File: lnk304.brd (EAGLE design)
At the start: 46 x 24 mm, 19 parts, among them IC1 TPS774, IC2 MCP1703CB

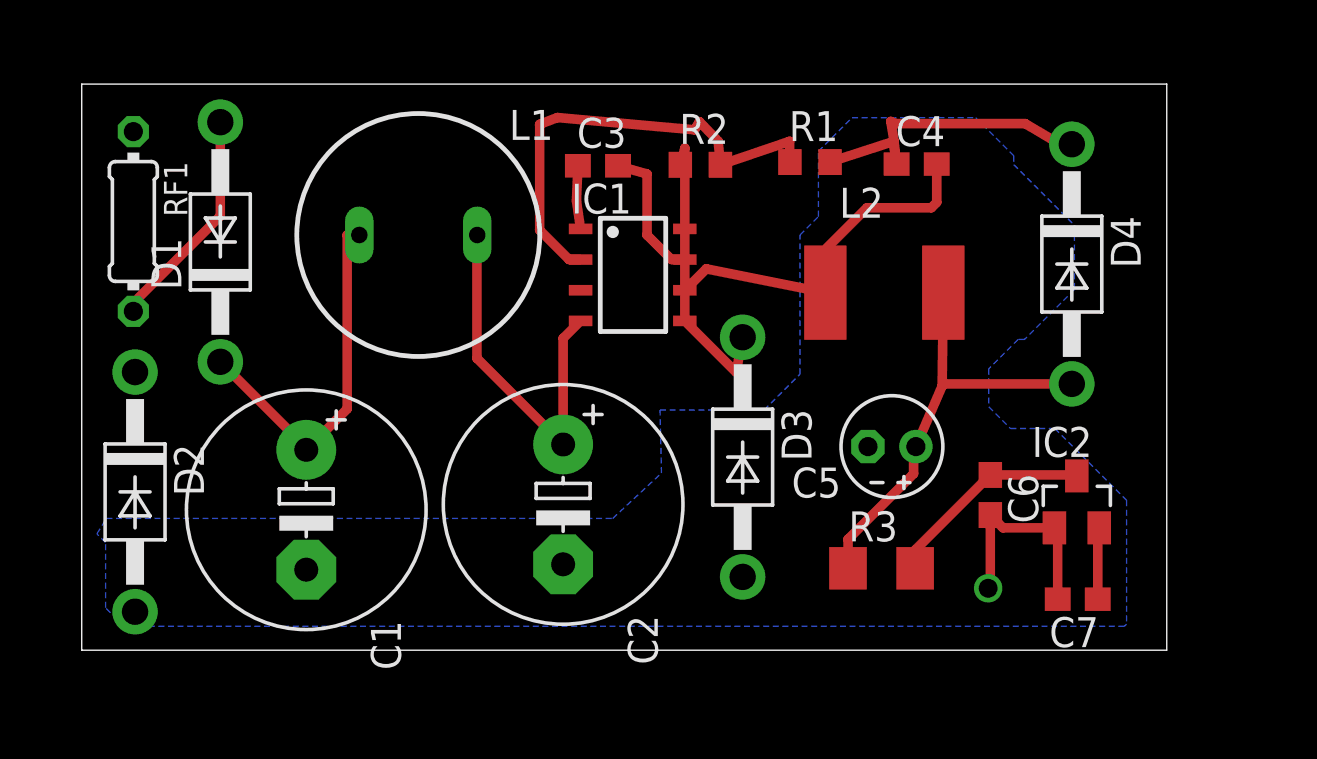
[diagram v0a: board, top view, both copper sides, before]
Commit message: Redesign to add Controller above the converter using pin headers
** 19.Mar.2016 **
Schematic:
- Change RF1 to fuse component
- Added Controller pin headers

PCB Layout:
- Increase board length from 46mm to 49.5mm
- Re orientation of components
RF1, D1, C1, C2, L2 R3 are the main components which were moved for long
distance
- Added Common Plane for Source pin of LNK

-- Missing --
- Need to revise Terminal Block size and overlapping with D2
- The LNK layout used till now is not the correct one.
- May need to increase L2 pad distance a bit
- May need to decrease the board height by 2mm

NOTE: Till now the design is just a fast draft. You can see that some
traces are not drawn in a clean way.
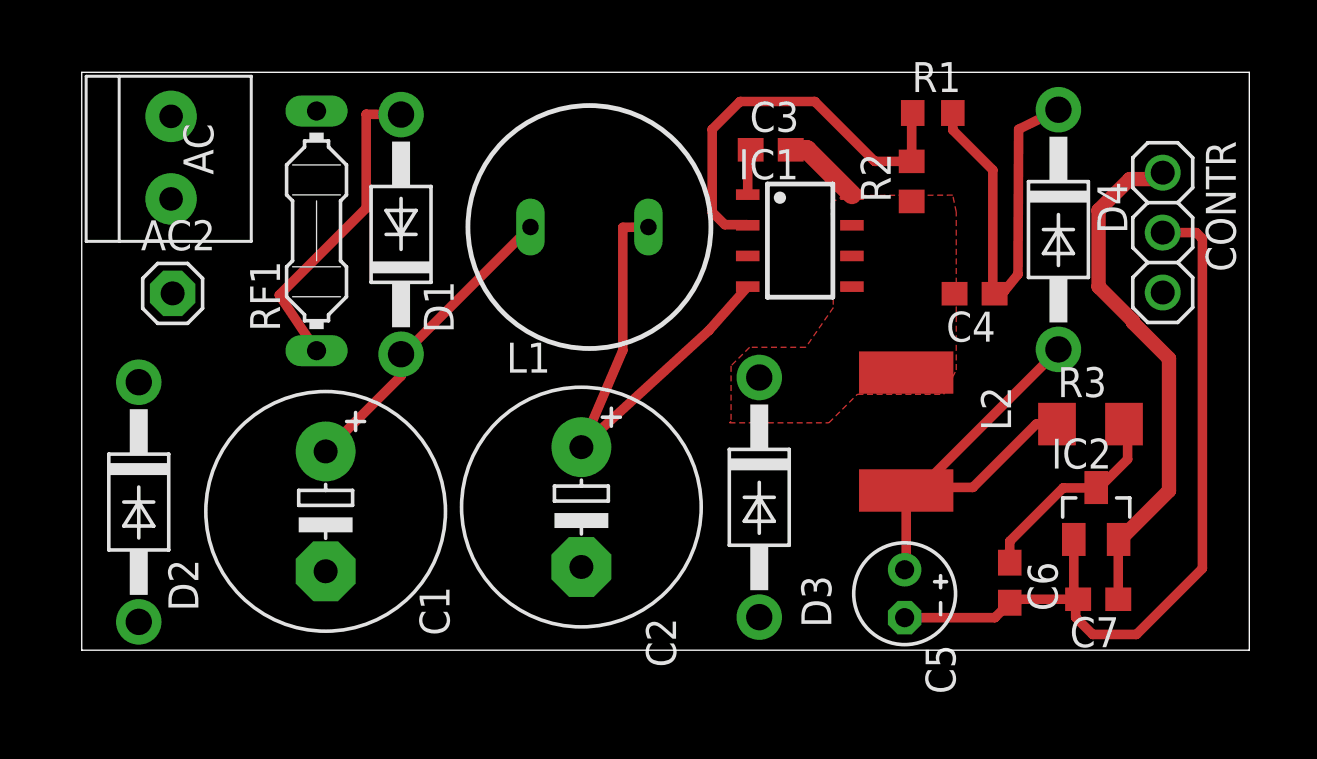
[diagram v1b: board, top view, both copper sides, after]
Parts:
- added AC: 1X2-3.5MM, adafruit:1X2-3.5MM
- added AC2: (no value), adafruit:1X01
- added CONTR: (no value), adafruit:1X03
- C1: value 4.7 uF 400 V -> 4.7 uF
- RF1: device resistor:0204/7 -> fuse:PICOFUSE
- moved R3 10.8 mm to (42.8, 9.59)
- moved R2 8.98 mm to (35.2, 19.9), turned to 90 degrees
- moved RF1 7.78 mm to (9.96, 17.8)
- moved D1 7.67 mm to (13.5, 17.6)
- moved C3 7.35 mm to (29.2, 21.2)
- moved L1 7.26 mm to (21.5, 17.9)
- moved IC1 7.23 mm to (30.4, 17.4)
- moved C5 6.26 mm to (34.9, 2.40), turned to 270 degrees
- moved C4 6.02 mm to (37.9, 15.1), turned to 180 degrees
- moved L2 5.96 mm to (35.0, 9.27), turned to 270 degrees
- moved R1 5.61 mm to (36.1, 22.8)
- moved C6 3.81 mm to (39.3, 2.86)
- moved D3 1.85 mm to (28.7, 6.48)
- moved D4 1.57 mm to (41.4, 17.8)
- moved IC2 0.96 mm to (43.0, 5.79)
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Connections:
- new net N$9: AC.2, RF1.1
- net GND: now also CONTR.2
- net N$14: now also CONTR.1
- net N$6: now also AC2.1
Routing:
- net N$8: track 34.0 -> 3.38 mm
- net GND: track 9.17 -> 33.7 mm, vias 1 -> 0
- net N$14: track 3.05 -> 22.0 mm
- net N$3: track 15.9 -> 20.6 mm
- net N$10: track 13.5 -> 17.9 mm
- net N$1: track 9.55 -> 13.5 mm
- net N$5: track 19.9 -> 17.3 mm
- net N$2: track 15.6 -> 13.2 mm
- net N$4: track 18.6 -> 19.5 mm
- net N$7: track 2.69 -> 1.95 mm
- added copper zone on layer 1, net N$8
- removed copper zone on layer 16, net GND
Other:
- board size 46 x 24 mm -> 49.5 x 24.5 mm

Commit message: Added 9v output pins
** 21.Mar.2016 **
Schematic:
- Added pin headers for 9v output which will be used by the relays
- Added extra ground pin to CONTR component

PCB Layout:
- Added pin headers for 9v output which will be used by the relays
- Added extra ground pin to CONTR component
- Added two 1mm holes
- Added Ground plane

Missing:
- Same issues
- Add Creepage between C1 and C2 pads
- Smash right side components and re organise the components names on
the silk screen
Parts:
- added 9VOUT: (no value), adafruit:1X03
- C2: value 4.7 uF 400 V -> 4.7 uF
- moved C6 0.69 mm to (39.6, 2.21)
- moved R3 0.55 mm to (43.3, 9.38)
- moved C7 0.51 mm to (43.1, 1.65)
- moved IC2 0.19 mm to (43.1, 5.93)
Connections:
- net GND: now also CONTR.3
- net N$4: now also 9VOUT.1, 9VOUT.2, 9VOUT.3
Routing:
- net GND: track 33.7 -> 10.7 mm
- net N$9: track 0.00 -> 6.26 mm
- net N$3: track 20.6 -> 14.8 mm
- net N$4: track 19.5 -> 22.9 mm
- net N$1: track 13.5 -> 11.6 mm
- net N$2: track 13.2 -> 14.5 mm
- net N$11: track 8.90 -> 9.52 mm
- net N$14: track 22.0 -> 22.7 mm
- added copper zone on layer 16, net GND
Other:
- board size 49.5 x 24.5 mm -> 48 x 24.5 mm

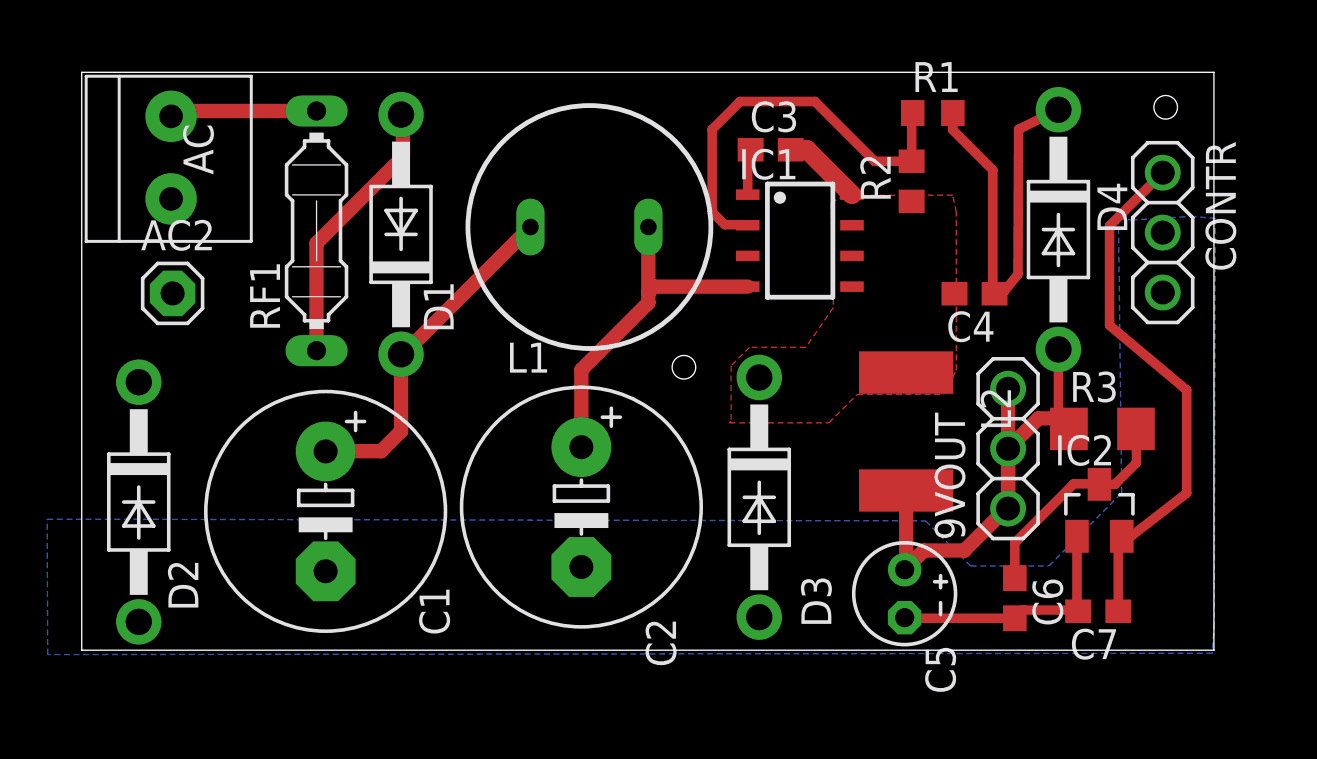
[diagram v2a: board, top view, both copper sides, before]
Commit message: Added the new package LNK30X
** 26.Mar.2016 **
- Checked in new file userdefined.lbr
- Created new device LNK30X
- The device has Symbol name LNK30X
- The device has Package name SO08C

Schematic:
- Added the new package LNK30X and rename component to LNK304

PCB Layout:
- Route the new package LNK30X
- Smash right side components and re organise the components names on
the silk screen
- Added two holes

-- Missing --
- Need to add hot and neutral pins for AC plug concept
- Need to revise Terminal Block size and overlapping with D2
- May need to increase L2 pad distance a bit
- May need to decrease the board height by 2mm
- Add Creepage between C1 and C2 pads
- Revise the two holes diameter and availability of screws
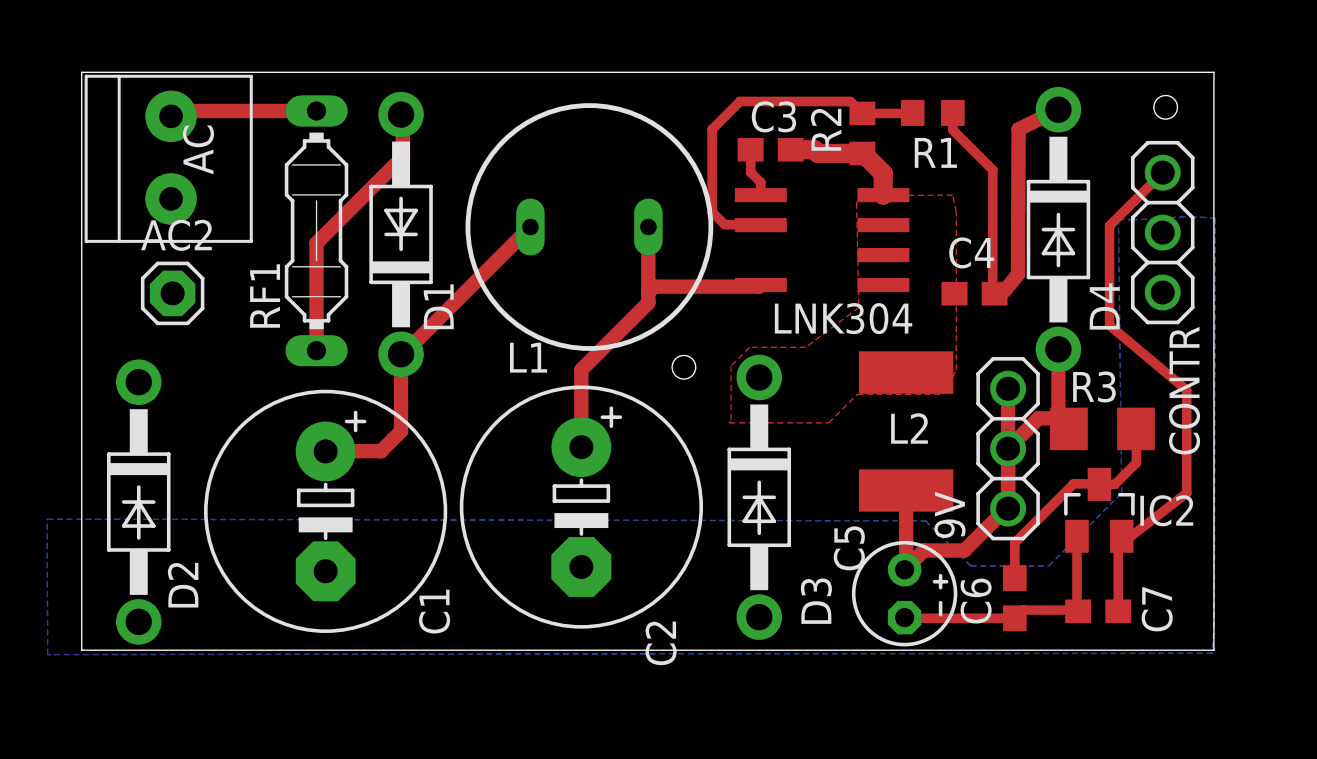
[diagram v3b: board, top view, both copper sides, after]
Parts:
- removed IC1: TPS774, texas:DGK-R-PDSO-G8
- added LNK304: (no value), userdefined:SO08
- C3: value 0.1 uF -> (none)
- C4: value 10 uF -> (none)
- C5: value 100 uF -> (none)
- C6, C7: value 1 uF -> (none)
- IC2: value MCP1703CB -> (none)
- R1: value 9.1k -> (none)
- R2: value 2k -> (none)
- R3: value 10 -> (none)
- moved R2 2.92 mm to (33.1, 21.9)
- renumbered 9VOUT to 9V
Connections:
- net N$3: now also LNK304.4; no longer IC1.4
- net N$5: now also LNK304.2; no longer IC1.2
- net N$7: now also LNK304.1; no longer IC1.1
- net N$8: now also LNK304.5, LNK304.6, LNK304.7, LNK304.8; no longer IC1.5, IC1.6, IC1.7, IC1.8
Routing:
- net N$5: track 17.3 -> 15.1 mm
- net N$8: track 3.38 -> 5.26 mm
- net N$3: track 14.8 -> 15.4 mm

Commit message: Added Bleeder resistor and varistor
** 26.Mar.2016 **
Schematic:
- Added a 1M 1/4Watt beelding resistor between hot and neutral
- Added Varistor VR1

PCB Layout:
- Change board height to 49.5mm
- Change trace width to 40mil
- Added a 1M 1/4Watt beelding resistor between hot and neutral
- Change layout of D2 to be shorter so that AC Terminal Block can fit
- Added Varistor VR1

-- Missing --
- Need to add hot and neutral pins for AC plug concept
- Need to revise Terminal Block size and overlapping with D2
- May need to increase L2 pad distance a bit
- May need to decrease the board height by 2mm
- Add Creepage between C1 and C2 pads
- Revise the two holes diameter and availability of screws

-- What can be changed --
- Hot and Neutral pins can be in one signale TBlock02 not 03
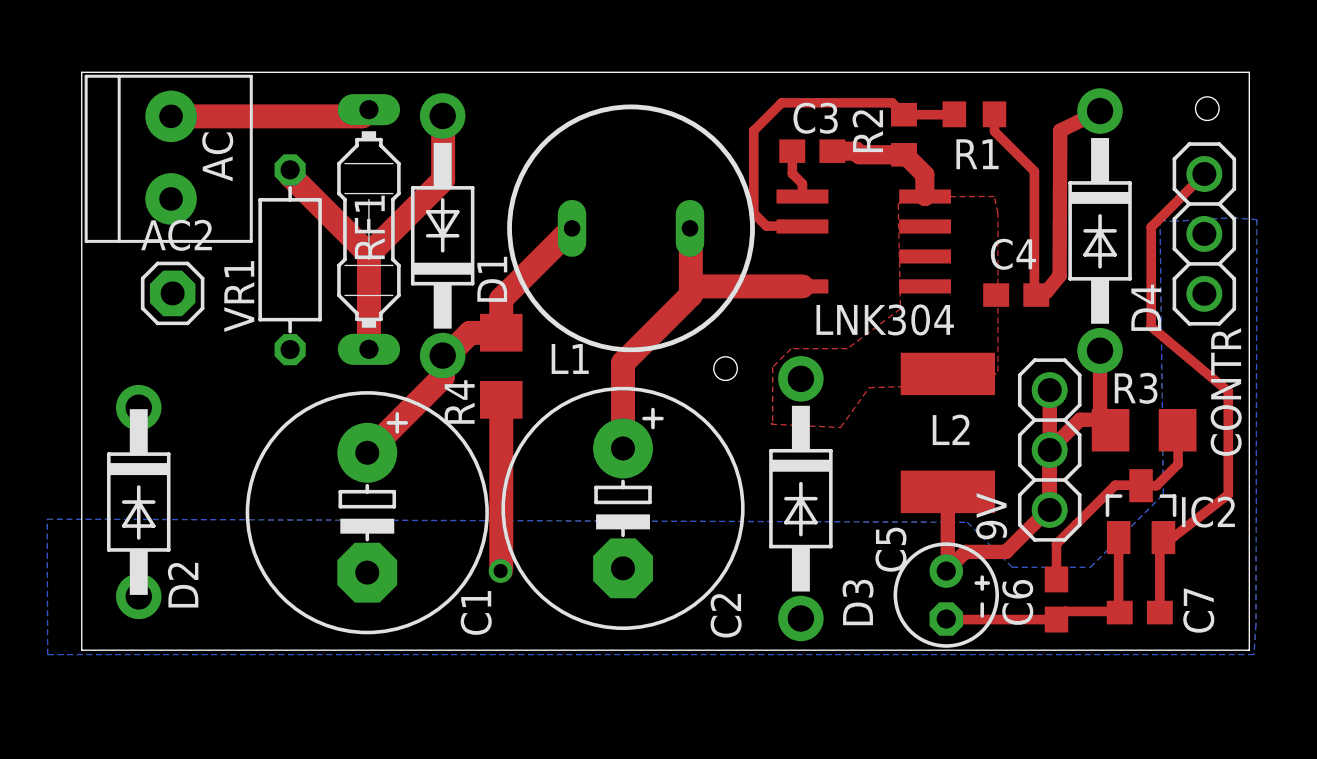
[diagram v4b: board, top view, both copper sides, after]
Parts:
- added R4: 10M, resistor:R1206
- added VR1: (no value), varistor:R-7,5
- D2: device adafruit:DO41-10 -> adafruit:DO41-7
- LNK304: device userdefined:SO08 -> userdefined:SO08C
- moved RF1 2.22 mm to (12.2, 17.8)
- moved C1 1.77 mm to (12.1, 5.83)
- moved C2 1.77 mm to (22.9, 6.01)
- moved C4 1.77 mm to (39.6, 15.1)
- moved C5 1.77 mm to (36.7, 2.34)
- moved C6 1.77 mm to (41.3, 2.15)
- moved CONTR 1.77 mm to (47.6, 17.6)
- moved D3 1.77 mm to (30.5, 6.42)
- moved IC2 1.77 mm to (44.9, 5.87)
- moved L1 1.77 mm to (23.3, 17.9)
- moved L2 1.77 mm to (36.7, 9.21)
- moved LNK304 1.77 mm to (33.2, 17.3)
- moved R2 1.77 mm to (34.9, 21.9)
- moved R3 1.77 mm to (45.0, 9.32)
- moved C3 1.77 mm to (31.0, 21.2)
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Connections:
- net GND: now also R4.1
- net N$1: now also VR1.1
- net N$2: now also R4.2
- net N$6: now also VR1.2
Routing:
- net GND: track 10.7 -> 17.9 mm, vias 0 -> 1
- net N$1: track 11.6 -> 16.2 mm
- net N$9: track 6.26 -> 8.51 mm
- net N$2: track 14.5 -> 14.0 mm
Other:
- board size 48 x 24.5 mm -> 49.5 x 24.5 mm
